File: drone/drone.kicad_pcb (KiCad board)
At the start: 2 copper layers, 40.5 x 40.5 mm, 45 parts, among them J3 Conn_01x03_Pin, U2 MPU-6050, U3 MP2303ADN

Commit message: ho
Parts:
- added +: TestPoint, TestPoint:TestPoint_Pad_2.5x2.5mm, B.Cu at (111.1, 101.6)
- added -: TestPoint, TestPoint:TestPoint_Pad_2.5x2.5mm, B.Cu at (114.8, 101.6)
- C5, C6, C7, C8, R3, R4, TP11, TP12, TP13, TP14, TP15, TP16, TP17, TP18, U2: moved to B.Cu
- moved TP17 149.9 mm to (83.0, 91.0), turned to 180 degrees
- moved TP15 148.6 mm to (83.0, 75.5), turned to 180 degrees
- moved TP14 143.6 mm to (83.0, 88.0), turned to 180 degrees
- moved TP12 143.1 mm to (83.0, 72.5), turned to 180 degrees
- moved TP10 137.3 mm to (83.0, 72.5)
- moved J3 134.3 mm to (86.0, 60.5), turned to 90 degrees
- moved TP5 132.2 mm to (83.0, 75.5)
- moved TP4 130.2 mm to (83.0, 88.0)
- moved TP3 130.0 mm to (83.0, 91.0)
- moved U2 125.6 mm to (104.0, 78.5), turned to 180 degrees
- moved R4 118.4 mm to (104.5, 73.5), turned to 90 degrees
- moved R2 116.5 mm to (106.5, 94.0)
- moved R3 115.7 mm to (107.0, 73.5), turned to 90 degrees
- moved R7 115.3 mm to (107.0, 91.5), turned to 180 degrees
- moved TP16 111.4 mm to (123.0, 73.0), turned to 180 degrees
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- renumbered TP1 to +, TP2 to -
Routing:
- net ESC VCC: track 3.76 -> 21.6 mm, vias 1 -> 11
- net +3V3: track 5.30 -> 15.8 mm, vias 0 -> 1
- net TX: track 0.00 -> 9.09 mm
- net RX: track 0.00 -> 5.69 mm
- net Batt Read: track 0.00 -> 5.22 mm
- net SDA: track 0.00 -> 2.75 mm
- net Net-(U2-CPOUT): track 0.00 -> 2.53 mm
- net Net-(U2-REGOUT): track 0.00 -> 2.51 mm
- net Net-(U3-SW): track 11.6 -> 9.28 mm
- net SCL: track 0.00 -> 2.18 mm
- net GND: vias 0 -> 9
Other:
- board size 40.5 x 40.5 mm -> 46 x 46 mm

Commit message: drc 0
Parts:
- +: renamed from TP10; moved to B.Cu
- +: renamed from TP8; moved to B.Cu
- +: renamed from TP4; moved to B.Cu
- +: renamed from TP6; moved to B.Cu
- -: renamed from TP9; moved to B.Cu
- -: renamed from TP7; moved to B.Cu
- -: renamed from TP3; moved to B.Cu
- -: renamed from TP5; moved to B.Cu
- ESC1: renamed from TP12; moved to F.Cu
- ESC2: renamed from TP14; moved to F.Cu
- ESC3: renamed from TP16; moved to F.Cu
- ESC4: renamed from TP18; moved to F.Cu
- LED: renamed from TP15; moved to F.Cu
- LED: renamed from TP17; moved to F.Cu
- LED: renamed from TP13; moved to F.Cu
- LED: renamed from TP11; moved to F.Cu
- NT1: moved to B.Cu
- moved - 0.12 mm to (114.8, 101.7)
- moved + 0.10 mm to (111.1, 101.7)
- moved TP1 0.10 mm to (111.1, 101.7)
- moved TP2 0.10 mm to (114.8, 101.7)
- moved + 0.10 mm to (123.0, 73.1), turned to 180 degrees
- moved - 0.10 mm to (123.0, 90.9), turned to 180 degrees
- moved LED 0.10 mm to (123.0, 90.9), turned to 0 degrees
- moved U1 0.06 mm to (103.8, 69.7)
- turned NT1 to 180 degrees
- turned + to 180 degrees (x3)
- turned - to 180 degrees (x3)
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- renumbered + to TP1, - to TP2
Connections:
- C12 pad 2: GND -> ESC GND
- C9 pad 2: GND -> ESC GND
- LED pad 1: GND -> ESC GND (x4)
- R11 pad 2: GND -> ESC GND
- R9 pad 2: GND -> ESC GND
- U3 pad 4: GND -> ESC GND
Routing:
- net ESC VCC: track 21.6 -> 135.9 mm
- net +3V3: track 15.8 -> 60.9 mm, vias 1 -> 3
- net ESC2: track 0.00 -> 21.6 mm
- net ESC4: track 0.00 -> 19.1 mm
- net ESC1: track 0.00 -> 13.2 mm
- net ESC3: track 0.00 -> 12.4 mm
- net Batt Read: track 5.22 -> 16.6 mm
- net SCL: track 2.18 -> 11.0 mm, vias 0 -> 1
- net GND: track 0.00 -> 6.12 mm, vias 9 -> 14
- net SDA: track 2.75 -> 8.05 mm, vias 0 -> 1
- net Net-(U3-FB): track 3.02 -> 5.52 mm
- net ESC GND: vias 0 -> 9
- added copper zone on B.Cu, net ESC GND
- added copper zone on F.Cu, net GND
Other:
- board text added: "GND"
- board text added: "RX"
- board text added: "TX"

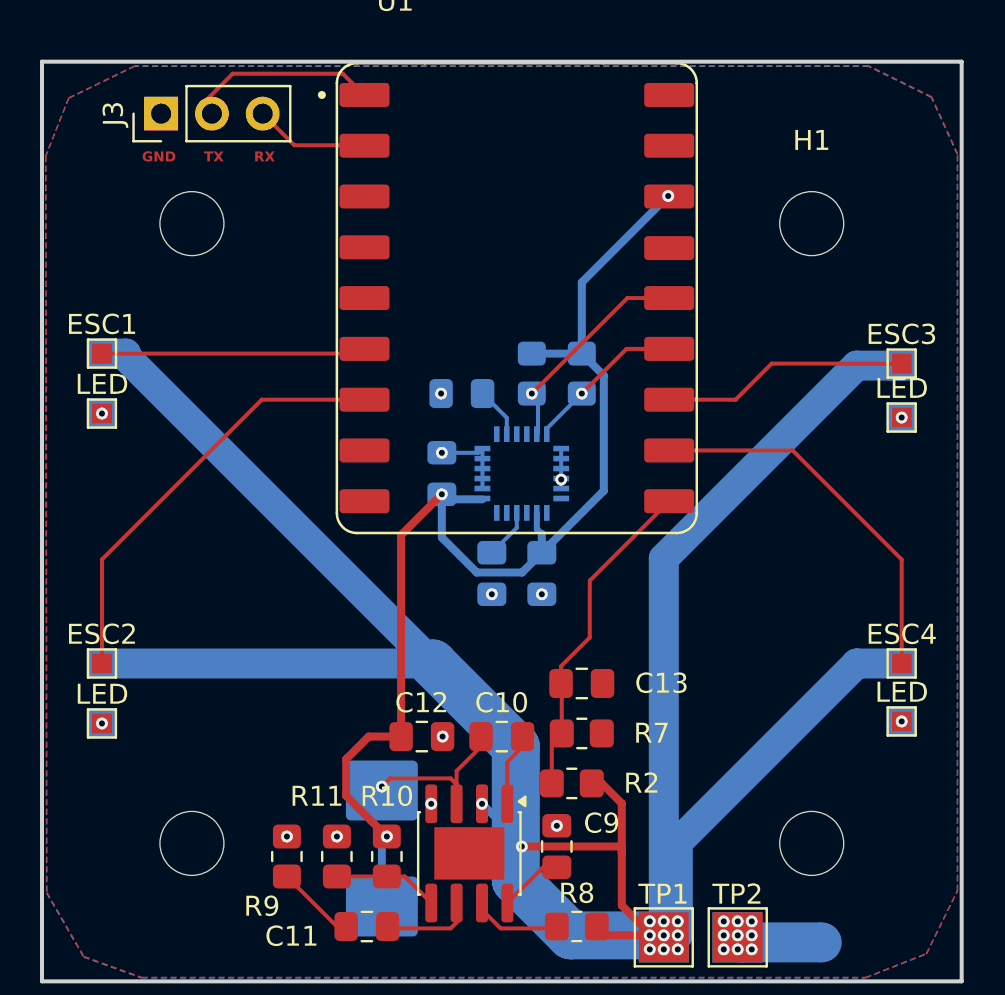
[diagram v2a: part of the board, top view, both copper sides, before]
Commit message: add buzzer
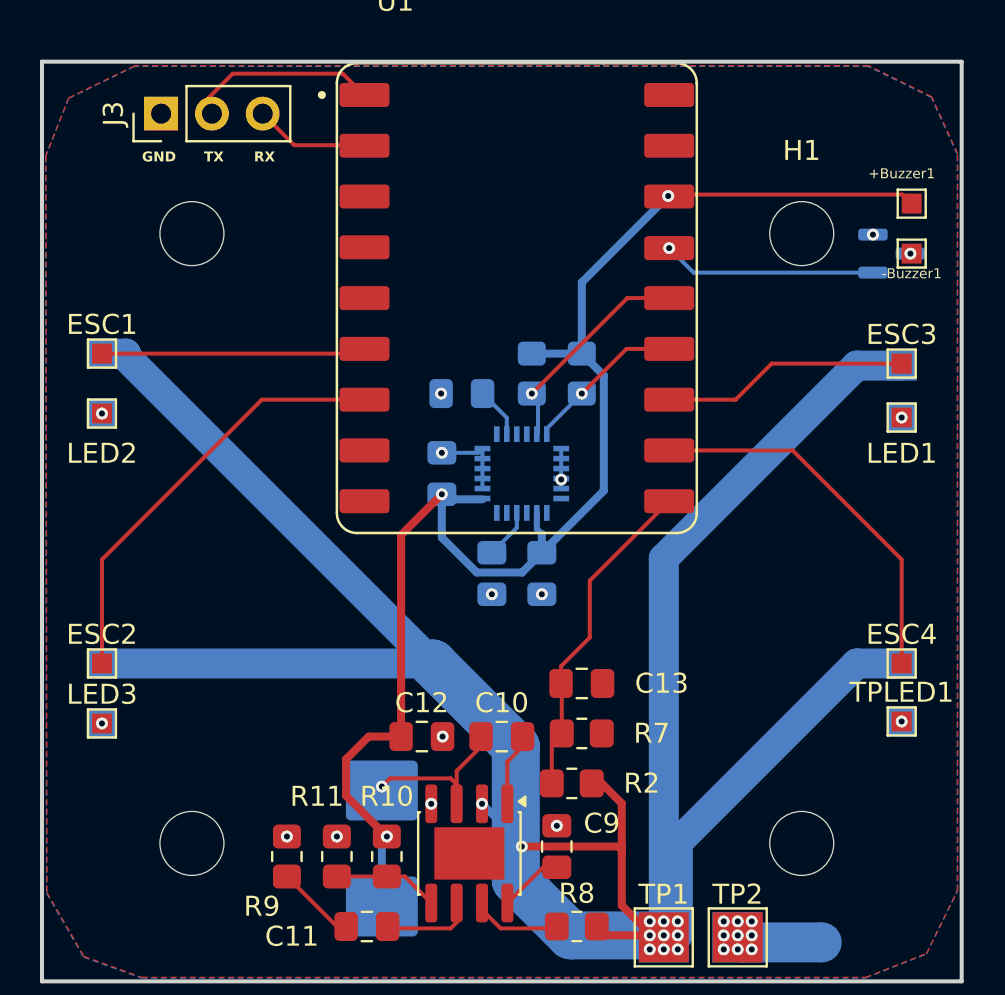
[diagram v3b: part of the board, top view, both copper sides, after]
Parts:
- added +Buzzer1: TestPoint, TestPoint:TestPoint_Pad_1.0x1.0mm, F.Cu at (123.5, 65.0)
- added -Buzzer1: TestPoint, TestPoint:TestPoint_Pad_1.0x1.0mm, F.Cu at (123.5, 67.5)
- added Q1: AO3400A, Package_TO_SOT_SMD:SOT-23, B.Cu at (122.5, 67.5)
- moved H1 0.71 mm to (118.0, 66.5)
- moved H3 0.50 mm to (118.0, 97.0)
- moved H4 0.50 mm to (87.5, 66.5)
- renumbered + to +1, + to +2, + to +3, + to +4, - to -1, - to -2, - to -3, - to -4, LED to LED1, LED to LED2, LED to LED3, - to TP19, + to TP20, LED to TPLED1
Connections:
- U1 pad 13: unconnected-(U1-GP13-Pad13) -> /Buzzer
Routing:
- net +3V3: track 60.9 -> 73.3 mm
- net /Buzzer: track 0.00 -> 10.7 mm, vias 0 -> 1
- net Net-(Q1-D): track 0.00 -> 0.06 mm, vias 0 -> 1
- net GND: vias 14 -> 15

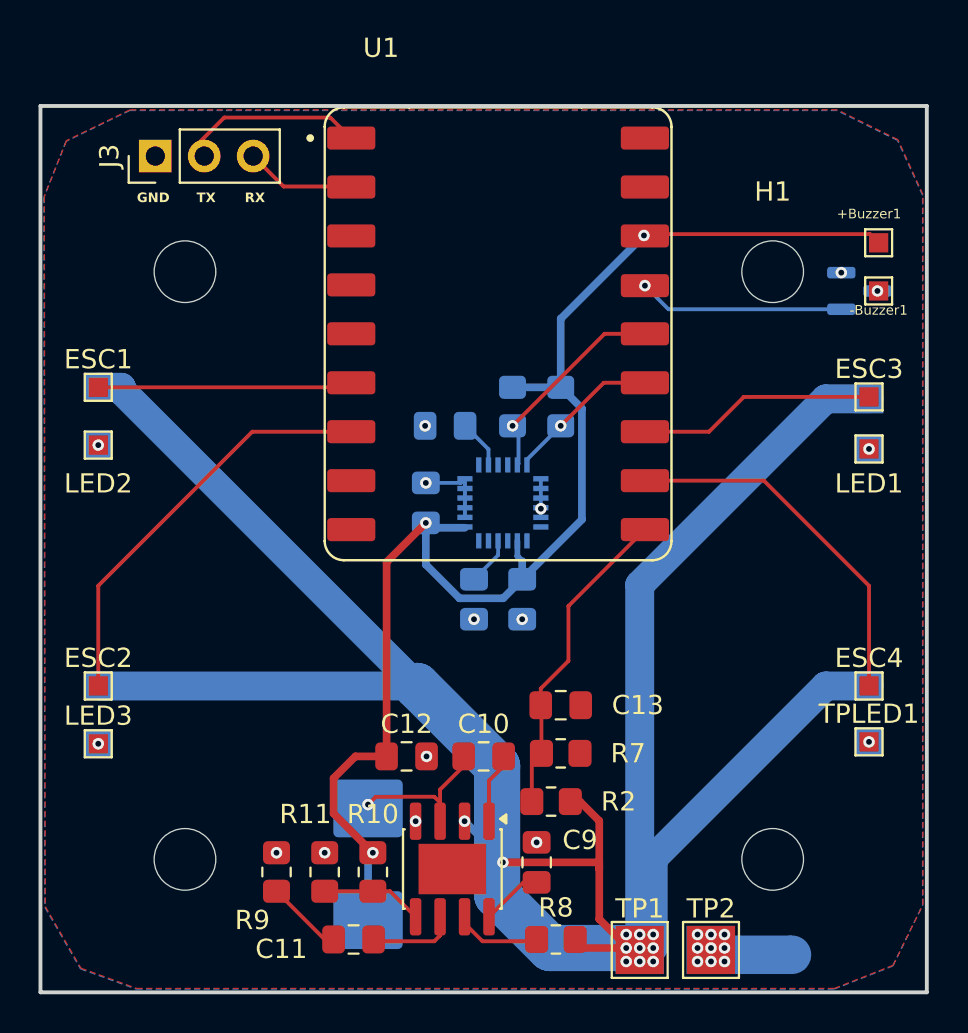
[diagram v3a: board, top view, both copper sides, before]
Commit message: silk + external uart + i2c
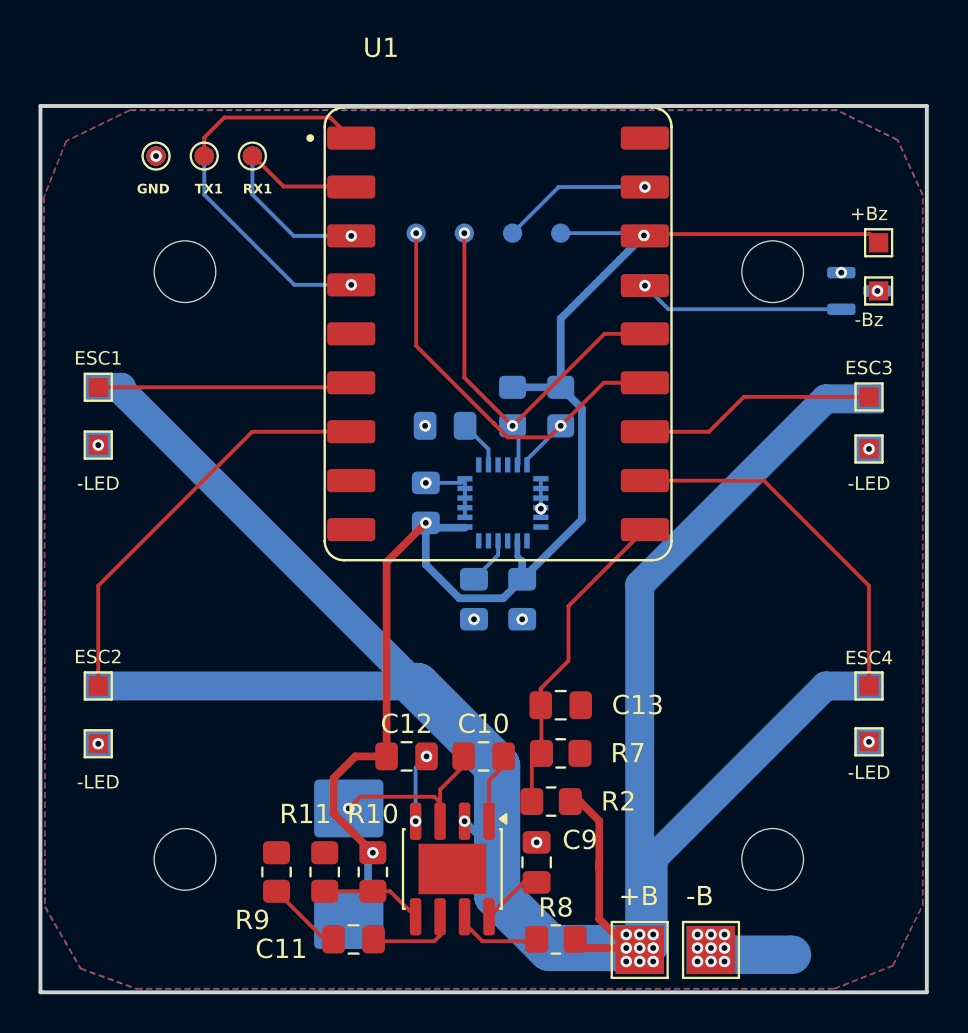
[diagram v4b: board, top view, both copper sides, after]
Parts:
- removed J3: Conn_01x03_Pin, Connector_PinHeader_2.54mm:PinHeader_1x03_P2.54mm_Vertical
- added -: TestPoint, TestPoint:TestPoint_Pad_D1.0mm, B.Cu at (104.5, 64.5)
- added 3v3: TestPoint, TestPoint:TestPoint_Pad_D1.0mm, B.Cu at (107.0, 64.5)
- added SCL: TestPoint, TestPoint:TestPoint_Pad_D1.0mm, B.Cu at (102.0, 64.5)
- added SDA: TestPoint, TestPoint:TestPoint_Pad_D1.0mm, B.Cu at (99.5, 64.5)
- added TP10: TestPoint, TestPoint:TestPoint_Pad_D1.0mm, B.Cu at (86.0, 60.5)
- added TP11: TestPoint, TestPoint:TestPoint_Pad_D1.0mm, B.Cu at (88.5, 60.5)
- added TP12: TestPoint, TestPoint:TestPoint_Pad_D1.0mm, B.Cu at (91.0, 60.5)
- added TP4: TestPoint, TestPoint:TestPoint_Pad_D1.0mm, F.Cu at (88.5, 60.5)
- added TP5: TestPoint, TestPoint:TestPoint_Pad_D1.0mm, F.Cu at (91.0, 60.5)
- added TP7: TestPoint, TestPoint:TestPoint_Pad_D1.0mm, F.Cu at (86.0, 60.5)
- moved L1 1.00 mm to (96.0, 97.3)
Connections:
- C12 pad 2: ESC GND -> GND
- R11 pad 2: ESC GND -> GND
- R9 pad 2: ESC GND -> GND
- U1 pad 1: unconnected-(U1-GP1-Pad1) -> RX2
- U1 pad 2: unconnected-(U1-GP2-Pad2) -> TX2
- U1 pad RX: RX -> RX1
- U1 pad TX: TX -> TX1
- U3 pad 4: ESC GND -> GND
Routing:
- net SDA: track 8.05 -> 23.7 mm, vias 1 -> 2
- net GND: track 6.12 -> 18.0 mm, vias 15 -> 19
- net TX2: track 0.00 -> 11.6 mm, vias 0 -> 1
- net SCL: track 11.0 -> 22.2 mm, vias 1 -> 2
- net TX1: track 0.00 -> 9.40 mm
- net TX: track 9.09 -> 0.00 mm
- net RX2: track 0.00 -> 8.02 mm, vias 0 -> 1
- net RX1: track 0.00 -> 5.69 mm
- net RX: track 5.69 -> 0.00 mm
- net ESC VCC: track 135.9 -> 130.9 mm, vias 11 -> 10
- net +3V3: track 73.3 -> 77.6 mm
- net Net-(U3-SW): track 9.28 -> 10.2 mm
- net ESC GND: vias 9 -> 5
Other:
- board text added: "+"
- board text added: "+B"
- board text added: "+Bz"
- board text added: "-"
- board text added: "-B"
- board text added: "-Bz"
- board text added: "-LED"
- board text added: "ESC1"
- board text added: "ESC2"
- board text added: "ESC3"
- board text added: "RX1"
- board text added: "RX2"
- board text added: "TX1"
- board text added: "TX2"
- board text removed: "RX"
- board text removed: "TX"

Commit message: drc = 0, jlcpcb matched
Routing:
- net /Buzzer: track 10.7 -> 12.3 mm
- net +3V3: track 77.6 -> 78.9 mm

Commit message: hi
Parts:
- added G***: LOGO, LOGO, B.Cu at (104.5, 92.5)
- R10: value 5.6K -> 22K
- R11: value 2.2K -> 4.7K
- moved TP3 4.00 mm to (104.5, 60.5)
- moved TP6 4.00 mm to (107.0, 60.5)
- moved TP8 4.00 mm to (102.0, 60.5)
- moved TP9 4.00 mm to (99.5, 60.5)
- moved Q1 1.20 mm to (123.0, 68.6), turned to 90 degrees
- moved +Buzzer1 0.50 mm to (123.0, 65.0)
- moved -Buzzer1 0.50 mm to (123.0, 67.5)
- renumbered - to TP3, 3v3 to TP6, SCL to TP8, SDA to TP9
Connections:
- C12 pad 1: +3V3 -> +5V
- L1 pad 1: +3V3 -> +5V
- R10 pad 2: +3V3 -> +5V
- U1 pad 4: ESC1 -> unconnected-(U1-GP4-Pad4)
- U1 pad 5: ESC2 -> unconnected-(U1-GP5-Pad5)
- U1 pad 5V: unconnected-(U1-Pad5V) -> +5V
- U1 pad 6: unconnected-(U1-GP6-Pad6) -> ESC1
- U1 pad 7: unconnected-(U1-GP7-Pad7) -> ESC2
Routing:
- net +5V: track 0.00 -> 56.3 mm, vias 0 -> 1
- net +3V3: track 78.9 -> 56.9 mm, vias 3 -> 1
- net ESC VCC: track 130.5 -> 136.8 mm
- net SCL: track 22.2 -> 26.2 mm
- net SDA: track 23.6 -> 27.6 mm
- net /Buzzer: track 12.3 -> 15.4 mm
- net ESC2: track 21.6 -> 19.5 mm
- net ESC1: track 13.2 -> 15.3 mm
- net GND: track 18.0 -> 18.9 mm
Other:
- board text added: "3V3"
- board text added: "SCL"
- board text added: "SDA"
- board text removed: "-Bz"

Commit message: them 5v
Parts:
- moved G*** 1.80 mm to (103.0, 91.5)
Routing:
- net +5V: track 56.3 -> 53.8 mm, vias 1 -> 3
- net /Buzzer: track 15.4 -> 16.5 mm
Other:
- board text added: "by TMADZ ver 1.0"

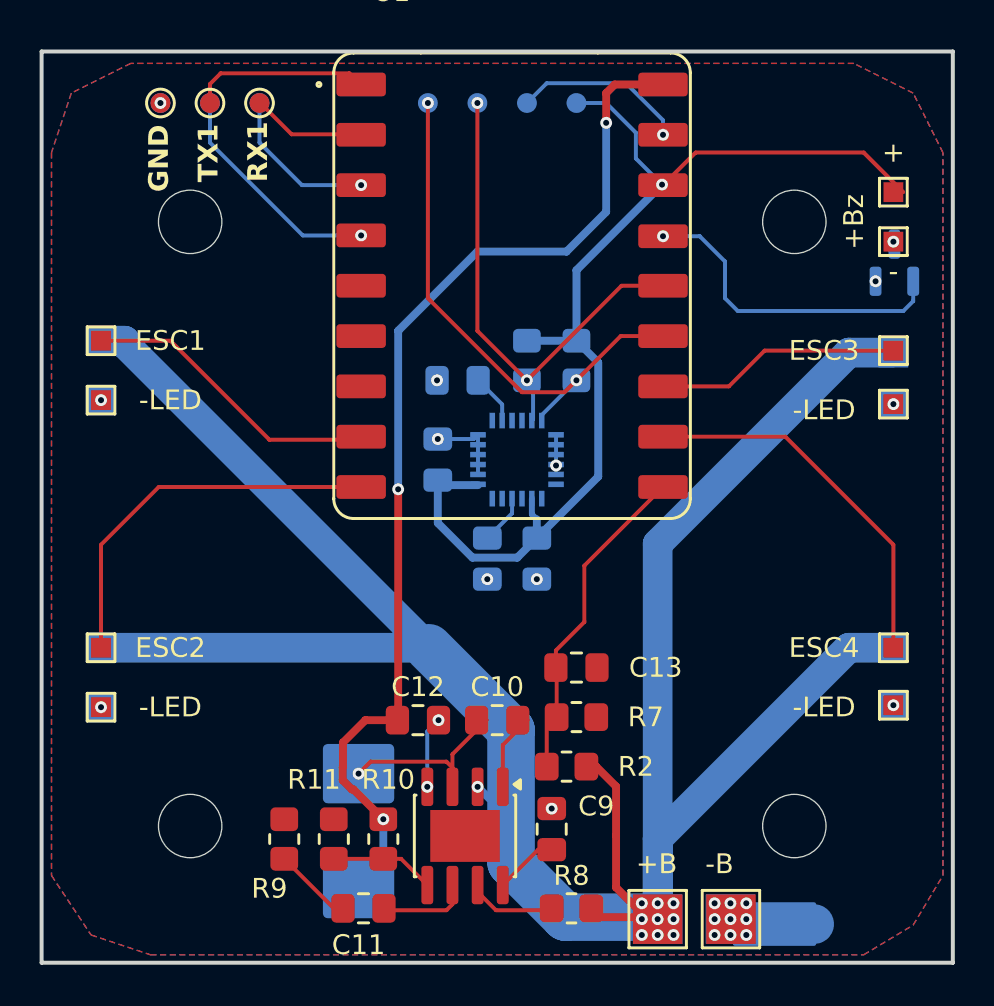
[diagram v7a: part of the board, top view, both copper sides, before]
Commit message: add ldo ams1117 3.3v
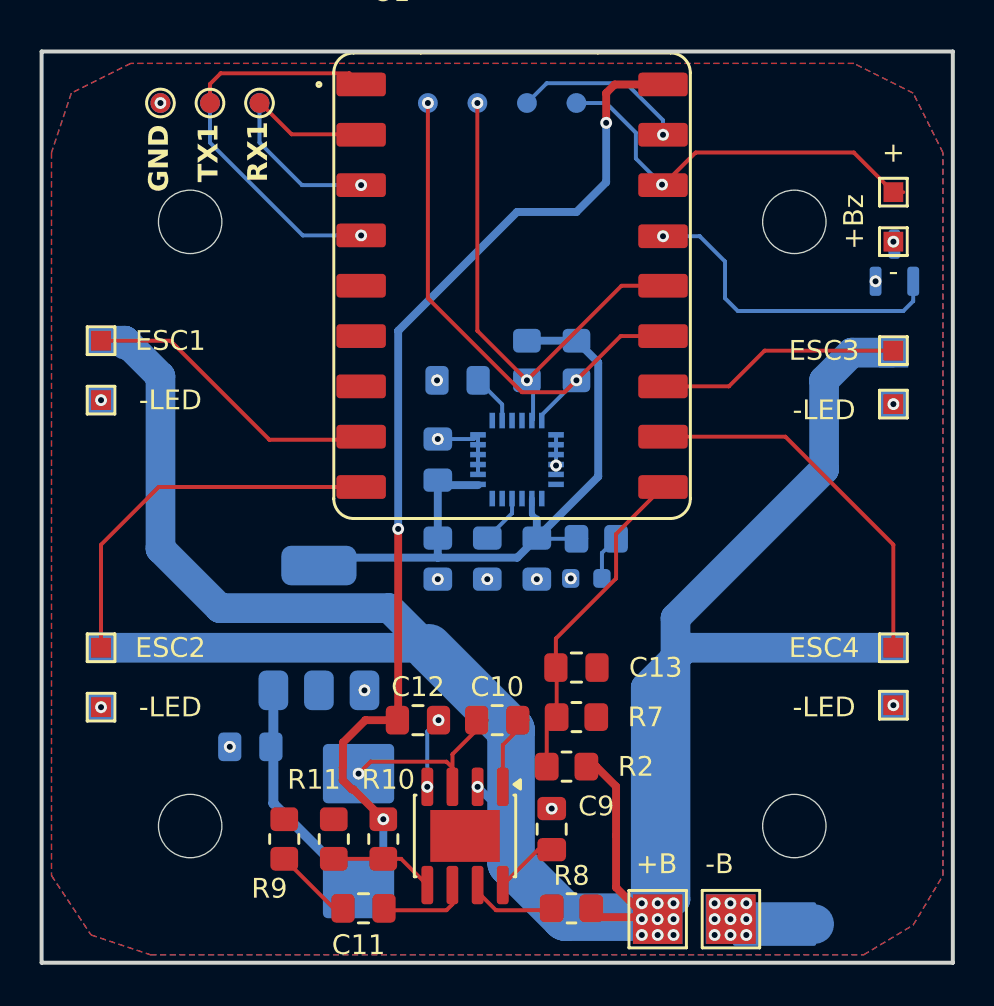
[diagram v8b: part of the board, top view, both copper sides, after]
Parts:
- added C14: 10uF, Capacitor_SMD:C_0805_2012Metric_Pad1.18x1.45mm_HandSolder, B.Cu at (90.5, 93.0)
- added C15: 10uF, Capacitor_SMD:C_0805_2012Metric_Pad1.18x1.45mm_HandSolder, B.Cu at (100.0, 83.5)
- added D1: LED, LED_SMD:LED_0603_1608Metric, B.Cu at (107.5, 84.5)
- added R5: 100, Resistor_SMD:R_0805_2012Metric_Pad1.20x1.40mm_HandSolder, B.Cu at (108.0, 82.5)
- added U4: AMS1117-3.3, Package_TO_SOT_SMD:SOT-223-3_TabPin2, B.Cu at (94.0, 87.0)
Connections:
- U1 pad 3V3: +3V3 -> unconnected-(U1-3V3(OUT)-Pad3V3)
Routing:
- net +5V: track 53.8 -> 64.7 mm
- net ESC VCC: track 136.8 -> 141.3 mm
- net Net-(D1-A): track 0.00 -> 2.30 mm
- net GND: vias 19 -> 23
